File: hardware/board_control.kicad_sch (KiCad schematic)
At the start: 47 parts, among them J10 Conn_01x02_Pin, J4 Conn_01x09_Pin

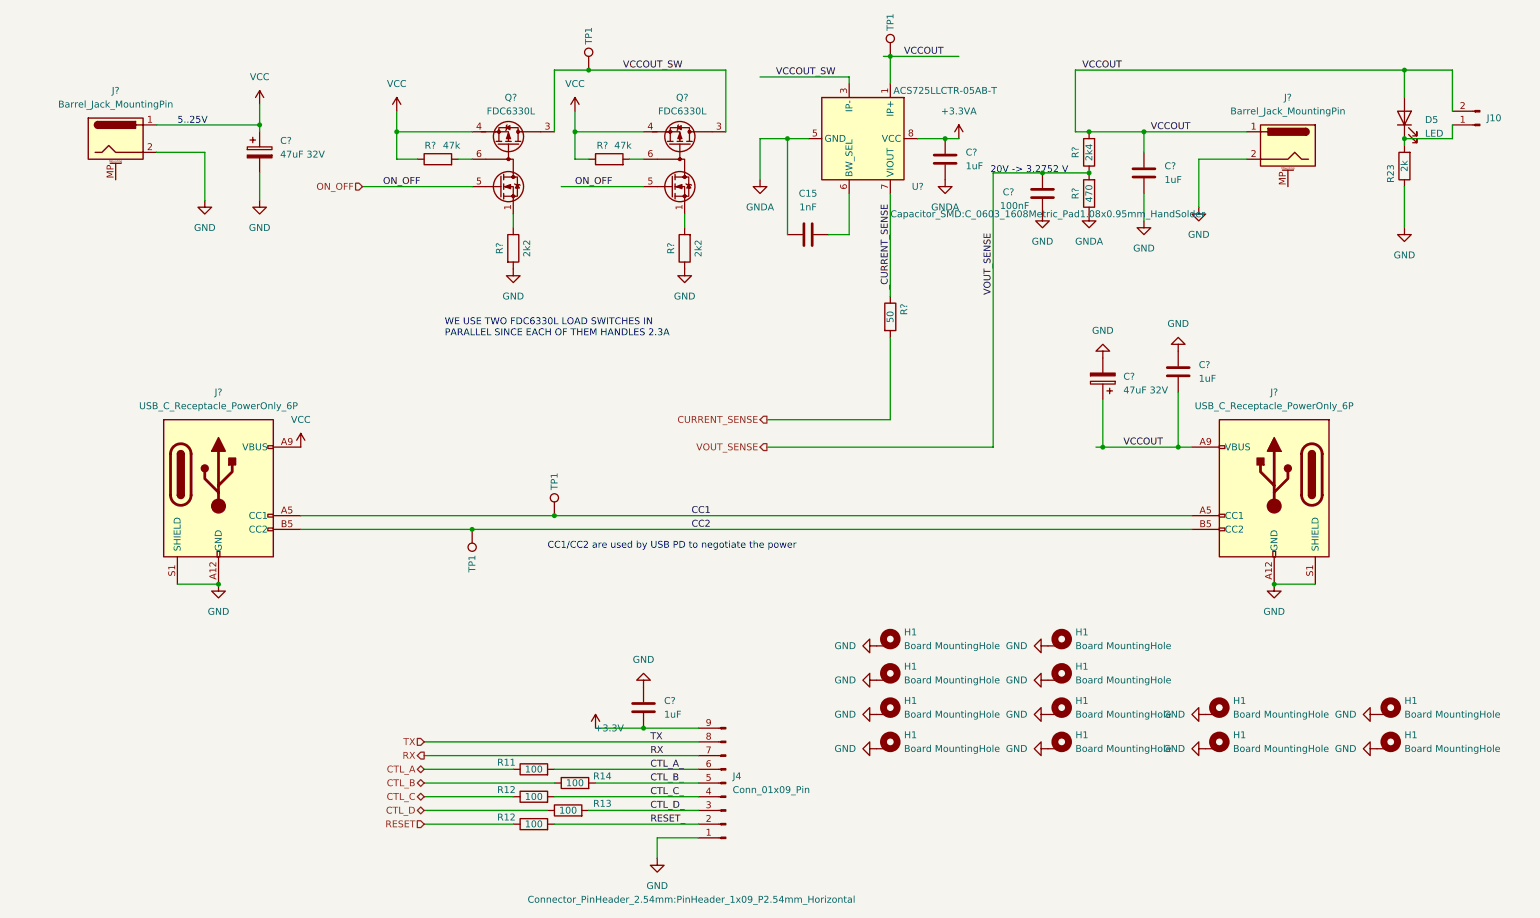
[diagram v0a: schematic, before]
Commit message: Started routing USB3 diff pairs
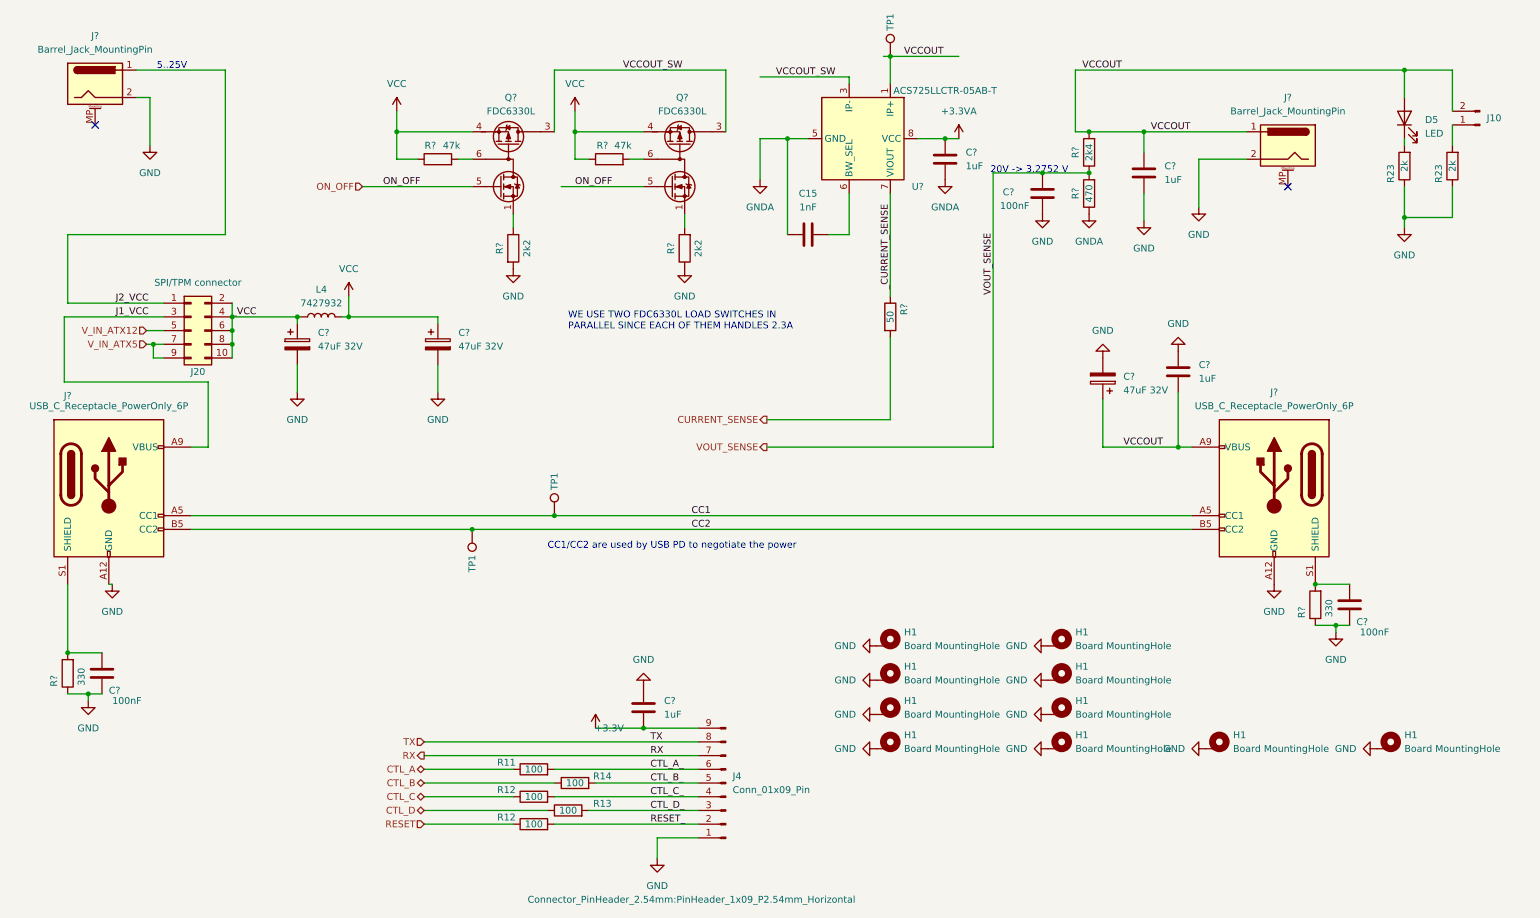
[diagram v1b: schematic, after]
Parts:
- removed C?: 47uF 32V, Capacitor_SMD:CP_Elec_6.3x5.4_Nichicon, symbol Device:C_Polarized
- removed H1 (x2): Board MountingHole, MountingHole:MountingHole_2.7mm_M2.5_Pad_Via, symbol Mechanical:MountingHole
- removed TP1: TestPoint, TestPoint:TestPoint_Pad_D1.0mm, symbol Connector:TestPoint
- added C? (x2): 47uF 32V, Capacitor_SMD:CP_Elec_6.3x5.4_Nichicon, symbol Device:C_Polarized
- added C? (x2): 100nF, Capacitor_SMD:C_0402_1005Metric, symbol Device:C
- added J20: SPI/TPM connector, Connector_PinHeader_2.54mm:PinHeader_2x05_P2.54mm_Vertical, symbol Connector_Generic:Conn_02x05_Odd_Even
- added L4: 7427932, FOOTPRINTS:7427932, symbol Device:L
- added R23: 2k, Resistor_SMD:R_0402_1005Metric, symbol Device:R
- added R? (x2): 330, Resistor_SMD:R_0402_1005Metric, symbol Device:R
- C15: footprint Capacitor_SMD:C_0603_1608Metric_Pad1.08x0.95mm_HandSolder -> Capacitor_SMD:C_0402_1005Metric
- C?: footprint Capacitor_SMD:C_0603_1608Metric_Pad1.08x0.95mm_HandSolder -> Capacitor_SMD:C_0402_1005Metric; MPN (none) -> CL05B104K05NNNC; MPN2 (none) -> TCC0402X7R104M160AT
- R11, R12, R13, R14, R23, R? (x7): footprint Resistor_SMD:R_0603_1608Metric -> Resistor_SMD:R_0402_1005Metric
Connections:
- net GND: now also C?.2, C?.2, C?.2, C?.2, R23.1, R?.1, R?.1; no longer J?.S1 (SHIELD), J?.S1 (SHIELD)
- net VCC: now also C?.1, L4.2; no longer J?.1, J?.A9 (VBUS), J?.B9 (VBUS)
- net at D5.1 (K), R23.2: no longer J10.1 (Pin_1)
- new net: J10.1 (Pin_1), R23.2
- new net: C?.1, J?.S1 (SHIELD), R?.2 (x2)
- new net J1_VCC: J20.3 (Pin_3), J?.A9 (VBUS), J?.B9 (VBUS)
- new net J2_VCC: J20.1 (Pin_1), J?.1
- new net V_IN_ATX12: J20.5 (Pin_5)
- new net V_IN_ATX5: J20.7 (Pin_7), J20.9 (Pin_9)
- new net _VCC: C?.1, J20.10 (Pin_10), J20.2 (Pin_2), J20.4 (Pin_4), J20.6 (Pin_6), J20.8 (Pin_8), L4.1
- no-connect marks 0 -> 2
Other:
- moved on the sheet: J?

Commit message: Continued routing
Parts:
- J? (x2): footprint Connector_USB:USB_C_Receptacle_G-Switch_GT-USB-7010ASV -> FOOTPRINTS:USB_C_Receptacle_G-Switch_GT-USB-7010ASV_fix
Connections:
- net GND: no longer C?.2
- net GNDA: now also C?.2
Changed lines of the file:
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@@
-    )
-  )
-  (symbol (lib_id "power:GND") (at 200.914 55.88 0) (unit 1)
-    (in_bom yes) (on_board yes) (dnp no) (fields_autoplaced)
-    (property "Reference" "#PWR?" (at 200.914 62.23 0)
-      (effects (font (size 1.27 1.27)) hide)
-    )
-    (property "Value" "GND" (at 200.914 60.96 0)
-      (effects (font (size 1.27 1.27)))
-    )
-    (property "Footprint" "" (at 200.914 55.88 0)
-      (effects (font (size 1.27 1.27)) hide)
-    )
-    (property "Datasheet" "" (at 200.914 55.88 0)
-      (effects (font (size 1.27 1.27)) hide)
-    )
-    (pin "1")
-    (instances
-      (project "jumpstarter"
-        (path "/5e49fb74-0a9b-4946-8b59-2b8244d10fd9"
-          (reference "#PWR?") (unit 1)
-        )
-        (path "/5e49fb74-0a9b-4946-8b59-2b8244d10fd9/0a246f5a-dd08-4f47-947a-3b89ae06d789"
-          (reference "#PWR045") (unit 1)
-        )
-      )
     )
   )
@@
       (effects (font (size 1.27 1.27)))
     )
-    (property "Footprint" "Connector_USB:USB_C_Receptacle_G-Switch_GT-USB-7010ASV" (at 31.75 104.14 0)
+    (property "Footprint" "FOOTPRINTS:USB_C_Receptacle_G-Switch_GT-USB-7010ASV_fix" (at 31.75 104.14 0)
       (effects (font (size 1.27 1.27)) hide)
     )
@@
     )
   )
+  (symbol (lib_id "power:GNDA") (at 200.914 55.88 0) (unit 1)
+    (in_bom yes) (on_board yes) (dnp no) (fields_autoplaced)
+    (property "Reference" "#PWR?" (at 200.914 62.23 0)
+      (effects (font (size 1.27 1.27)) hide)
+    )
+    (property "Value" "GNDA" (at 200.914 60.96 0)
+      (effects (font (size 1.27 1.27)))
+    )
+    (property "Footprint" "" (at 200.914 55.88 0)
+      (effects (font (size 1.27 1.27)) hide)
+    )
+    (property "Datasheet" "" (at 200.914 55.88 0)
+      (effects (font (size 1.27 1.27)) hide)
+    )
+    (pin "1")
+    (instances
+      (project "jumpstarter"
+        (path "/5e49fb74-0a9b-4946-8b59-2b8244d10fd9"
+          (reference "#PWR?") (unit 1)
+        )
+        (path "/5e49fb74-0a9b-4946-8b59-2b8244d10fd9/0a246f5a-dd08-4f47-947a-3b89ae06d789"
+          (reference "#PWR045") (unit 1)
+        )
+      )
+    )
+  )
   (symbol (lib_id "Device:C") (at 257.81 128.27 0) (unit 1)
     (in_bom yes) (on_board yes) (dnp no)
@@
       (effects (font (size 1.27 1.27)))
     )
-    (property "Footprint" "Connector_USB:USB_C_Receptacle_G-Switch_GT-USB-7010ASV" (at 240.03 104.14 0)
-      (effects (font (size 1.27 1.27)) hide)
-    )
+    (property "Footprint" "FOOTPRINTS:USB_C_Receptacle_G-Switch_GT-USB-7010ASV_fix" (at 240.03 104.14 0)
+      (effects (font (size 1.27 1.27)) hide)
+    )

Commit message: Almost ready 2.0.0
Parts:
- C15: Link (none) -> https://eu.mouser.com/ProductDetail/YAGEO/CC0402KRX7R0BB102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; MFN (none) -> CC0402KRX7R0BB102; MPN (none) -> CC0402KRX7R0BB102
- C? (x3): MFN (none) -> HV470M035E055ETR; MPN (none) -> HV470M035E055ETR
- C? (x4): footprint Capacitor_SMD:C_0603_1608Metric_Pad1.08x0.95mm_HandSolder -> Capacitor_SMD:C_0603_1608Metric; MFN (none) -> CL10B105KA8NNNC; MPN (none) -> CL10B105KA8NNNC
- C? (x3): MFN (none) -> CL10B104KB8NNNC
- D5: MFN (none) -> LTST-C190KRKT; MPN (none) -> LTST-C190KRKT
- J10: MFN (none) -> PZ254V-11-02P; MPN (none) -> PZ254V-11-02P
- J20: MFN (none) -> A2541WV-2X5P
- J4: MFN (none) -> A2541WR-9P; MPN (none) -> A2541WR-9P
- J? (x2): Link (none) -> https://www.lcsc.com/product-detail/USB-Connectors_G-Switch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; MFN (none) -> GT-USB-7010ASV; MPN (none) -> GT-USB-7010ASV
- J? (x2): MFN (none) -> DC-005B-2.5A-2.5; MPN (none) -> DC-005B-2.5A-2.5
- L4: Link (none) -> https://www2.mouser.com/ProductDetail/Wurth-Elektronik/7427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; MFN (none) -> 7427932; MPN (none) -> 7427932
- Q? (x2): Link (none) -> https://www.mouser.es/ProductDetail/onsemi-Fairchild/FDC633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; MFN (none) -> FDC6330L; MPN (none) -> FDC6330L
- R11, R12, R13, R14: MFN (none) -> RTT021000FTH; MPN (none) -> RTT021000FTH
- R23: MFN (none) -> RTT02202JTH; MPN (none) -> RTT02202JTH
- R?: value 2k4 -> 2k4 1%; MFN (none) -> AC0402FR-072K4L; MPN (none) -> AC0402FR-072K4L
- R? (x2): MFN (none) -> RTT024702FTH; MPN (none) -> RTT024702FTH
- R?: value 470 -> 470 1%; MFN (none) -> RTT024700FTH; MPN (none) -> RTT024700FTH
- R?: MFN (none) -> RC0402JR-0750RL; MPN (none) -> RC0402JR-0750RL
- R? (x2): MFN (none) -> RTT02331JTH; MPN (none) -> RTT02331JTH
- R? (x2): MFN (none) -> RTT022201FTH; MPN (none) -> RTT022201FTH
- U?: Link (none) -> https://eu.mouser.com/ProductDetail/Allegro-MicroSystems/AC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; MFN (none) -> ACS725LLCTR-05AB-T; MPN (none) -> ACS725LLCTR-05AB-T
